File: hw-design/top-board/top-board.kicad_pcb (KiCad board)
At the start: 2 copper layers, 170 x 66.6 mm, 131 parts, among them P1 POWER_CONN, P2 ISP, P4 BOTTOM_CONN, P5 BACKLIGHT, P6 BACKLIGHT, P7 FOOTSWITCH, P8 FOOTSWITCH, Q1 2N7002, Q2 MMBT2222A, Q3 MMBT2222A, SW1 BT_RESET, U1 NCP1117DT50G, U2 NCP1117DT33G, U3 MCP6001, U4 LPC1759FBD80, U5 PCA9685, Y1 10MHz

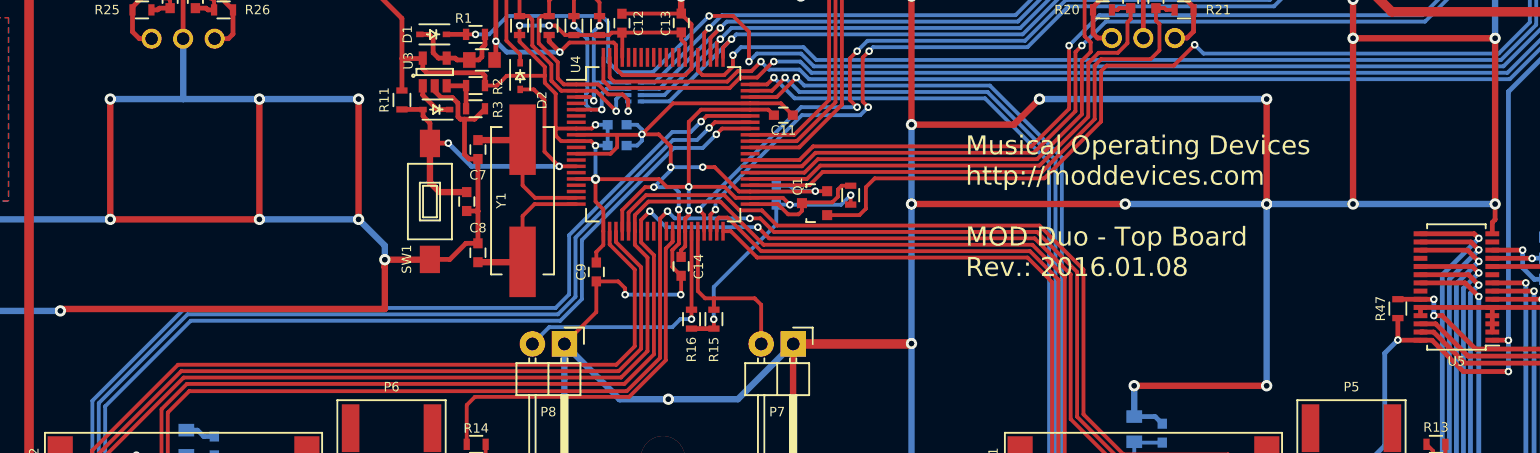
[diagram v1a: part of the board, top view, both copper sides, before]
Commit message: added logo's and updated gerber files
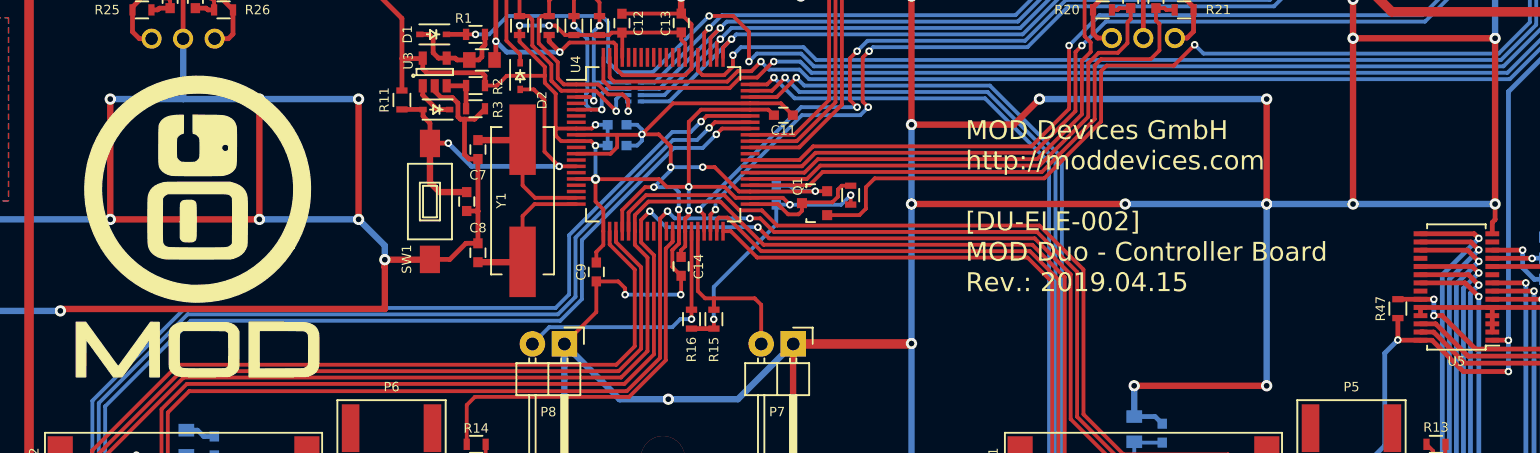
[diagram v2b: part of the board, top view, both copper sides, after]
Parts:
- added G***: LOGO, footprints:mod-logo, F.Cu at (119.7, 70.7)
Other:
- board text added: "MOD Devices GmbH http://moddevices.com [DU-ELE-002] MOD Duo - Controller Board Rev.: 2019.04.15"
- board text removed: "Musical Operating Devices http://moddevices.com MOD Duo - Top Board Rev.: 2016.01.08"
